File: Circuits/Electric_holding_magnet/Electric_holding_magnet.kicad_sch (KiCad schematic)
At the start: 9 parts, among them J1 Conn_01x03, Q1 BC547, Q2 BC547, SW1 SW_DIP_x01

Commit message: udated footprints npn
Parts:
- H1, H2: value (none) -> MountingHole_Pad; footprint (none) -> MountingHole:MountingHole_2.2mm_M2_DIN965_Pad
- Q1: footprint Package_TO_SOT_THT:TO-92_Inline -> (none)
- Q2: value BC547 -> (none); footprint Package_TO_SOT_THT:TO-92_Inline -> (none)
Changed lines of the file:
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@@
       (effects (font (size 1.27 1.27)) (justify left))
     )
-    (property "Value" "" (id 1) (at 163.83 64.7699 0)
+    (property "Value" "MountingHole_Pad" (id 1) (at 163.83 64.7699 0)
       (effects (font (size 1.27 1.27)) (justify left))
     )
-    (property "Footprint" "" (id 2) (at 161.29 64.77 0))
+    (property "Footprint" "MountingHole:MountingHole_2.2mm_M2_DIN965_Pad" (id 2) (at 161.29 64.77 0))
     (property "Datasheet" "~" (id 3) (at 161.29 64.77 0)
       (effects (font (size 1.27 1.27)) hide)
@@
       (effects (font (size 1.27 1.27)) (justify left))
     )
-    (property "Footprint" "Package_TO_SOT_THT:TO-92_Inline" (id 2) (at 137.16 83.185 0)
+    (property "Footprint" "" (id 2) (at 137.16 83.185 0)
       (effects (font (size 1.27 1.27) italic) (justify left) hide)
     )
@@
       (effects (font (size 1.27 1.27)) (justify left))
     )
-    (property "Value" "BC547" (id 1) (at 154.94 92.7099 0)
+    (property "Value" "" (id 1) (at 154.94 92.7099 0)
       (effects (font (size 1.27 1.27)) (justify left))
     )
-    (property "Footprint" "Package_TO_SOT_THT:TO-92_Inline" (id 2) (at 154.94 93.345 0)
+    (property "Footprint" "" (id 2) (at 154.94 93.345 0)
       (effects (font (size 1.27 1.27) italic) (justify left) hide)
     )
@@
       (effects (font (size 1.27 1.27)) (justify left))
     )
-    (property "Value" "" (id 1) (at 93.98 96.5199 0)
+    (property "Value" "MountingHole_Pad" (id 1) (at 93.98 96.5199 0)
       (effects (font (size 1.27 1.27)) (justify left))
     )
-    (property "Footprint" "" (id 2) (at 91.44 96.52 0)
+    (property "Footprint" "MountingHole:MountingHole_2.2mm_M2_DIN965_Pad" (id 2) (at 91.44 96.52 0)
       (effects (font (size 1.27 1.27)) hide)
     )
@@
     )
     (path "/7f52d787-caa3-4a92-b1b2-19d554dc29a4"
-      (reference "Q1") (unit 1) (value "BC547") (footprint "Package_TO_SOT_THT:TO-92_Inline")
+      (reference "Q1") (unit 1) (value "BC547") (footprint "Package_TO_SOT_THT:TO-92_HandSolder")
     )
     (path "/90e410ad-8466-4f6d-aba5-640aff7389dc"
-      (reference "Q2") (unit 1) (value "BC547") (footprint "Package_TO_SOT_THT:TO-92_Inline")
+      (reference "Q2") (unit 1) (value "BC547") (footprint "Package_TO_SOT_THT:TO-92_HandSolder")
     )
     (path "/d4fe307e-1033-4241-963d-fdbaaa45a5e9"

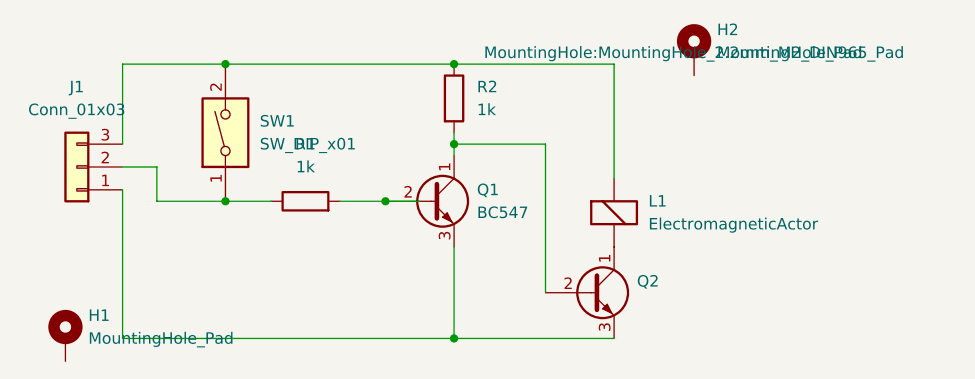
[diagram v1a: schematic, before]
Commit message: update pnp footprint
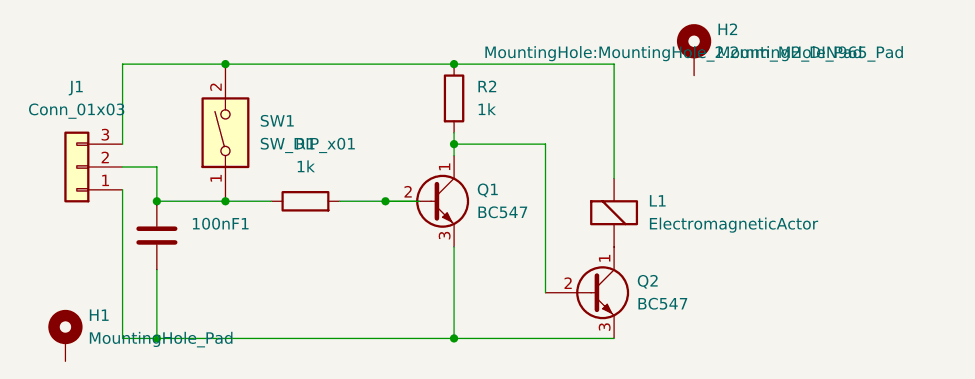
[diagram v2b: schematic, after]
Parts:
- added 100nF1: (no value), symbol Device:C
- Q1: footprint (none) -> Package_TO_SOT_THT:TO-92_HandSolder
- Q2: value (none) -> BC547; footprint (none) -> Package_TO_SOT_THT:TO-92_HandSolder
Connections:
- net at J1.1 (Pin_1), Q1.3 (E), Q2.3 (E): now also 100nF1.2
- net at J1.2 (Pin_2), R1.1, SW1.1: now also 100nF1.1
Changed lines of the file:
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@@
 (kicad_sch (version 20211123) (generator eeschema)
   (paper "A4")
+  (junction (at 101.6 96.52) (diameter 0) (color 0 0 0 0)
+  )
   (junction (at 134.62 66.04) (diameter 0) (color 0 0 0 0)
   )
   (junction (at 134.62 74.93) (diameter 0) (color 0 0 0 0)
   )
+  (junction (at 101.6 81.28) (diameter 0) (color 0 0 0 0)
+  )
   (junction (at 109.22 66.04) (diameter 0) (color 0 0 0 0)
   )
@@
     (stroke (width 0) (type default) (color 0 0 0 0))
   )
+  (wire (pts (xy 101.6 88.9) (xy 101.6 96.52))
+    (stroke (width 0) (type default) (color 0 0 0 0))
+  )
   (wire (pts (xy 97.79 74.93) (xy 97.79 66.04))
     (stroke (width 0) (type default) (color 0 0 0 0))
@@
     (stroke (width 0) (type default) (color 0 0 0 0))
   )
-  (wire (pts (xy 97.79 96.52) (xy 134.62 96.52))
+  (wire (pts (xy 97.79 96.52) (xy 101.6 96.52))
     (stroke (width 0) (type default) (color 0 0 0 0))
   )
@@
   (wire (pts (xy 134.62 74.93) (xy 144.78 74.93))
     (stroke (width 0) (type default) (color 0 0 0 0))
+  )
+  (wire (pts (xy 101.6 96.52) (xy 134.62 96.52))
+    (stroke (width 0) (type default) (color 0 0 0 0))
+  )
+  (symbol (lib_id "Device:C") (at 101.6 85.09 0) (unit 1)
+    (in_bom yes) (on_board yes) (fields_autoplaced)
+    (property "Reference" "100nF1" (id 0) (at 105.41 83.8199 0)
+      (effects (font (size 1.27 1.27)) (justify left))
+    )
+    (property "Value" "" (id 1) (at 105.41 86.3599 0)
+      (effects (font (size 1.27 1.27)) (justify left))
+    )
+    (property "Footprint" "" (id 2) (at 102.5652 88.9 0)
+      (effects (font (size 1.27 1.27)) hide)
+    )
+    (property "Datasheet" "~" (id 3) (at 101.6 85.09 0)
+      (effects (font (size 1.27 1.27)) hide)
+    )
+    (pin "1")
+    (pin "2")
   )
   (symbol (lib_id "Device:ElectromagneticActor") (at 152.4 83.82 0) (unit 1)
@@
       (effects (font (size 1.27 1.27)) (justify left))
     )
-    (property "Footprint" "" (id 2) (at 137.16 83.185 0)
+    (property "Footprint" "Package_TO_SOT_THT:TO-92_HandSolder" (id 2) (at 137.16 83.185 0)
       (effects (font (size 1.27 1.27) italic) (justify left) hide)
     )
@@
       (effects (font (size 1.27 1.27)) (justify left))
     )
-    (property "Value" "" (id 1) (at 154.94 92.7099 0)
-      (effects (font (size 1.27 1.27)) (justify left))
-    )
-    (property "Footprint" "" (id 2) (at 154.94 93.345 0)
+    (property "Value" "BC547" (id 1) (at 154.94 92.7099 0)
+      (effects (font (size 1.27 1.27)) (justify left))
+    )
+    (property "Footprint" "Package_TO_SOT_THT:TO-92_HandSolder" (id 2) (at 154.94 93.345 0)
       (effects (font (size 1.27 1.27) italic) (justify left) hide)
     )
@@
   )
   (symbol_instances
+    (path "/2276bf47-b441-4aa2-ba22-8213875ce0ee"
+      (reference "100nF1") (unit 1) (value "C") (footprint "Capacitor_THT:C_Disc_D5.0mm_W2.5mm_P2.50mm")
+    )
     (path "/ede4beab-a9a5-4c09-acb1-3acf6320bb10"
       (reference "H1") (unit 1) (value "MountingHole_Pad") (footprint "MountingHole:MountingHole_2.2mm_M2_DIN965_Pad")
